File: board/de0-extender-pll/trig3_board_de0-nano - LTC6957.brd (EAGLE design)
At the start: 160 x 75 mm, 92 parts, among them J12 4p-2.54, J13 BU-SMB-V, J17 2p-2.54, J23 2p-2.54, J24 2p-2.54, J3 4p-2.54, J32 2p-2.54, J33 2p-2.54, J34 2p-2.54, J38 2p-2.54, J39 2p-2.54, J42 2p-2.54, J43 2p-2.54, J5 2p-2.54, J6 2p-2.54, J7 4p-2.54, K15_R10P BU-SMB-V, K16_R10N BU-SMB-V, P11 BU-SMB-V, P15 BU-SMB-V, P16_R15N BU-SMB-V, P9 BU-SMB-V, T13_B20N BU-SMB-V, T9CLK_7N BU-SMB-V

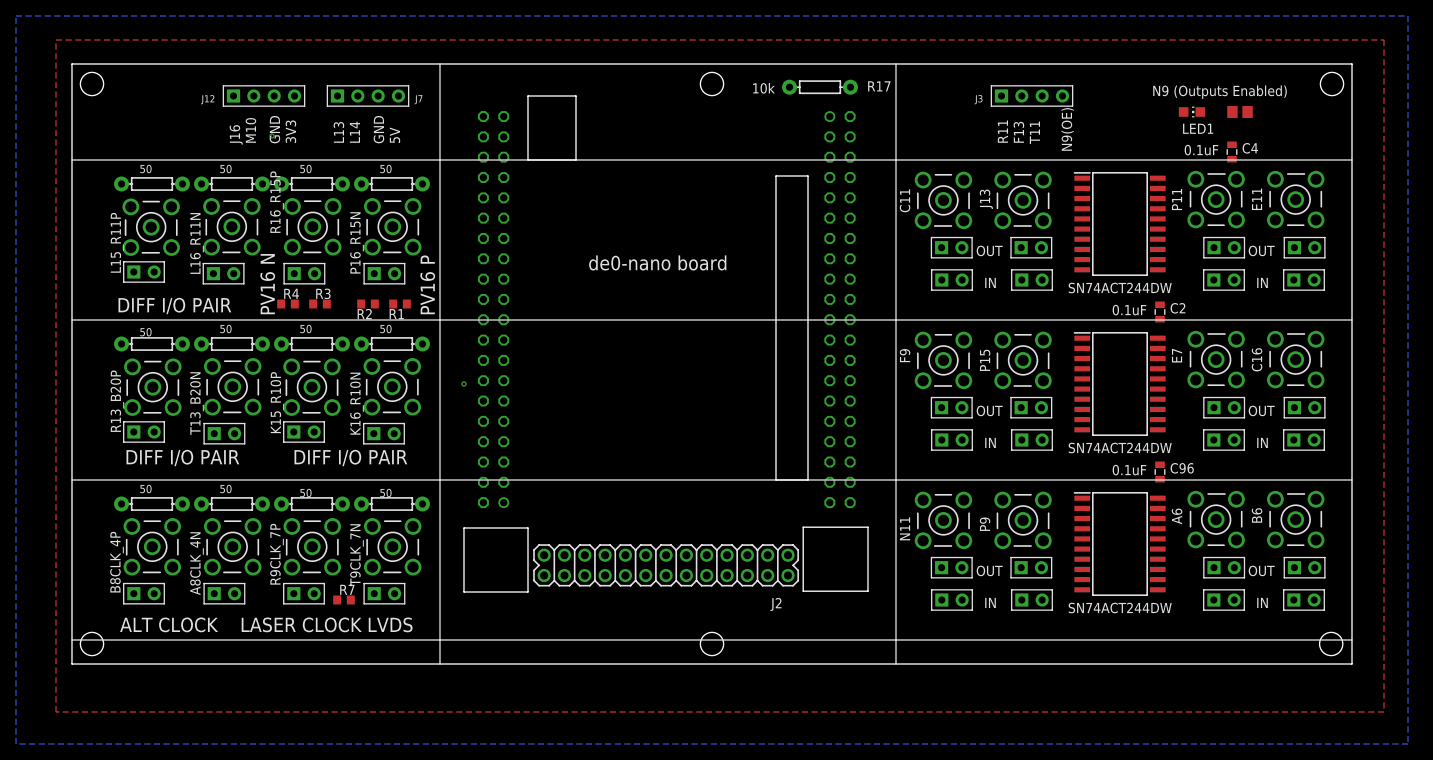
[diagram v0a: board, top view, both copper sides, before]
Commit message: fixed pecl termination
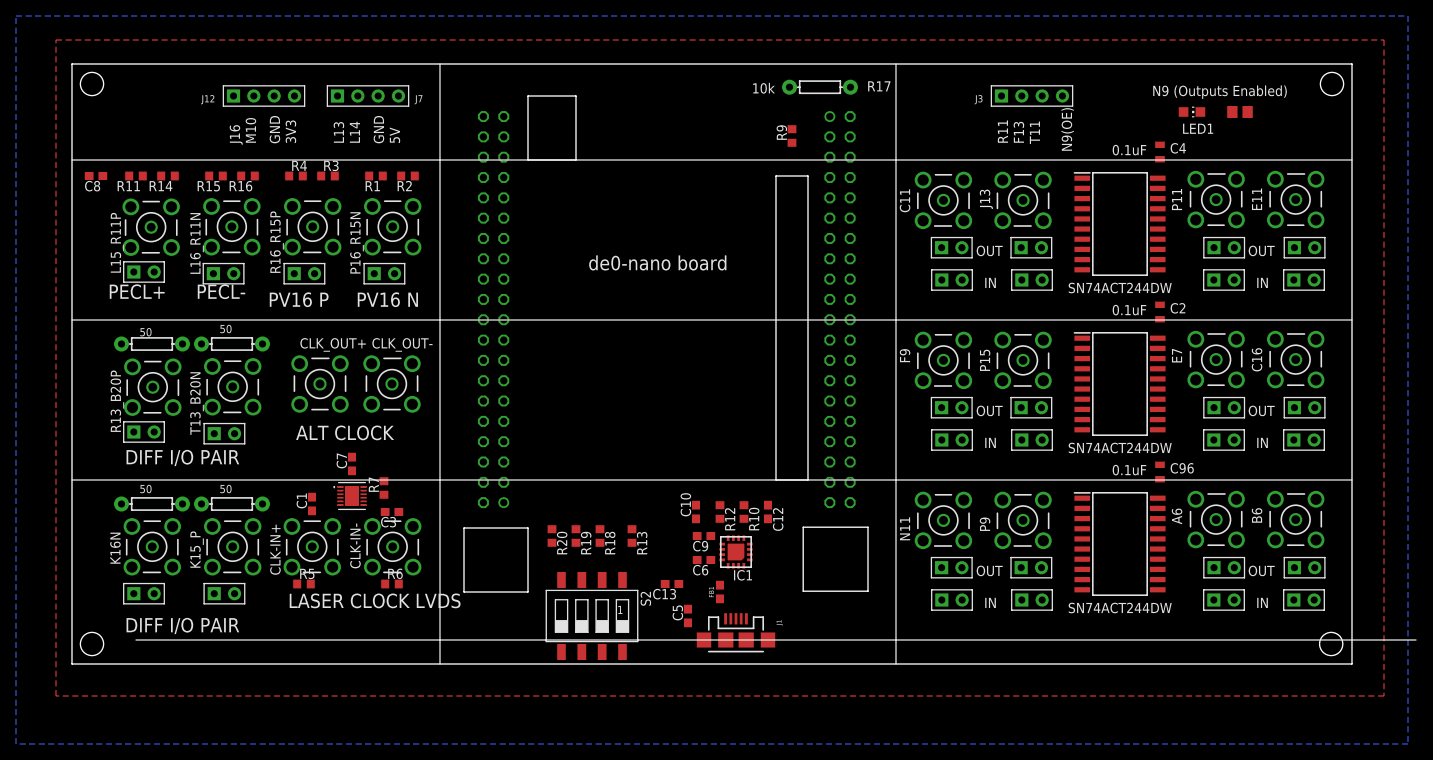
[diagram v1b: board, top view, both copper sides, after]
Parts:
- removed J2: (no value), SparkFun-Connectors:2X13
- removed J33, J39, J5, J6: 2p-2.54, Seeed-Connector:H2-2.54
- removed K15_R10P, K16_R10N: BU-SMB-V, con-coax:BU-SMB-V
- removed R28, R30, R31, R35, R41, R43: 50, SparkFun-Passives:AXIAL-0.3
- added C1, C3: 10 nF, rcl:C0603
- added C10, C12: 47pF, rcl:C0603
- added C13: 4.7 uF, rcl:C0603
- added C5, C6, C7, C8, C9: 0.1 uF, rcl:C0603
- added CLK_OUT+, CLK_OUT-: BU-SMB-V, con-coax:BU-SMB-V
- added FB1: 30Ω, SparkFun-Coils:0603
- added IC1: FT230XQ, ftdichip:QFN16
- added J1: (no value), SparkFun-Connectors:USB-MICROB
- added R10, R12: 27, rcl:R0603
- added R11, R16: 83, rcl:R0603
- added R13, R18, R19, R20: 330k, rcl:R0603
- added R14, R15: 130, rcl:R0603
- added R9: 100, rcl:R0603
- added S2: SWS004, smd-special:SMS-004
- added U1: LTC6957IDD-2TRPBF, ltc6957-2:DFN-12_DD_LIT
- R5, R6: value 50 -> 49.9; device SparkFun-Passives:AXIAL-0.3 -> rcl:R0603
- moved R2 16.8 mm to (-3.00, 97.0)
- moved R1 16.3 mm to (-7.00, 97.0)
- moved R3 16.0 mm to (-13.0, 97.0)
- moved R4 16.0 mm to (-17.0, 97.0)
- moved R7 14.9 mm to (-6.00, 58.0), turned to 90 degrees
- moved R5 10.0 mm to (-16.0, 46.0), turned to 0 degrees
- moved R6 10.0 mm to (-5.00, 46.0), turned to 0 degrees
- moved C4 9.00 mm to (91.0, 100.0)
- renumbered A8CLK_4N to K15_P, B8CLK_4P to K16N, R9CLK_7P to CLK-IN+, T9CLK_7N to CLK-IN-
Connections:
- new net N$1: J17.1, R13_B20P.2, R13_B20P.3, R13_B20P.4, R13_B20P.5, R161.P$1
- new net N$11: C10.2, J1.D-, R12.1
- new net N$12: IC1.6, R10.2
- new net N$13: IC1.7, R12.2
- new net N$14: C9.1, IC1.1, IC1.8, IC1.9
- new net N$15: R13.2, S2.1, U1.1
- new net N$16: R18.2, S2.2, U1.6
- new net N$17: R19.2, S2.3, U1.12
- new net N$18: R20.2, S2.4, U1.7
- new net N$2: C1.1, CLK-IN+.1, R5.2
- new net N$3: C3.1, CLK-IN-.1, R6.2
- new net N$4: C1.2, U1.3
- new net N$5: C3.2, U1.4
- new net N$6: C5.2, FB1.1, J1.VBUS
- new net N$7: C12.1, J1.D+, R10.1
- net 3V3: now also C7.1, C8.1, R14.1, R15.2, R4.1, S2.5, S2.6, S2.7, S2.8, U1.2; no longer R3.2
- net 5V: now also C13.1, C6.1, FB1.2, IC1.10
- net GND: now also C10.1, C12.2, C13.2, C5.1, C6.2, C7.2, C8.2, C9.2, CLK_OUT+.2, CLK_OUT+.3, CLK_OUT+.4, CLK_OUT+.5, CLK_OUT-.2, CLK_OUT-.3, CLK_OUT-.4, CLK_OUT-.5, IC1.13, IC1.2, IC1.3, J1.GND, R11.2, R13.1, R16.1, R18.1, R19.1, R20.1, R3.2, R5.1, R6.1, U1.13, U1.5; no longer J17.1, J33.1, J39.1, J5.1, J6.1, K15_R10P.2, K15_R10P.3, K15_R10P.4, K15_R10P.5, K16_R10N.2, K16_R10N.3, K16_R10N.4, K16_R10N.5, R13_B20P.2, R13_B20P.3, R13_B20P.4, R13_B20P.5, R161.P$1, R28.P$1, R30.P$1, R31.P$1, R35.P$1, R4.1, R41.P$1, R43.P$1, R5.P$1, R6.P$1
- net GPIO_0_IN0_A8CLK: now also CLK_OUT-.1, R9.2, U1.9; no longer J24.2, K15_P.1, R23.P$2
- net GPIO_0_IN1_B8CLK: now also CLK_OUT+.1, R9.1, U1.8; no longer J23.2, K16N.1, R22.P$2
- net GPIO_116_L16: now also R15.1, R16.2; no longer R28.P$2
- net GPIO_117_K16: now also J23.2, K16N.1, R22.P$2; no longer J33.2, K16_R10N.1, R30.P$2
- net GPIO_118_R16: no longer R31.P$2
- net GPIO_119_L15: now also R11.1, R14.2; no longer R43.P$2
- net GPIO_121_P16: no longer R41.P$2
- net GPIO_130_J16: now also IC1.15
- net GPIO_131_K15: now also J24.2, K15_P.1, R23.P$2; no longer J39.2, K15_R10P.1, R35.P$2
- net GPIO_1_IN0_T9CLK: now also U1.10; no longer CLK-IN-.1, J6.2, R6.P$2
- net GPIO_1_IN1_R9CLK: now also U1.11; no longer CLK-IN+.1, J5.2, R5.P$2
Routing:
- net GPIO_131_K15: track 53.1 -> 0.00 mm, vias 1 -> 0
- net GPIO_1_IN1_R9CLK: track 27.3 -> 0.00 mm
- net GPIO_118_R16: track 24.9 -> 0.00 mm
- net GPIO_117_K16: track 20.7 -> 0.00 mm, vias 1 -> 0
- net GPIO_1_IN0_T9CLK: track 16.2 -> 0.00 mm
- net GPIO_121_P16: track 11.9 -> 0.00 mm
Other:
- board text added: "PECL+"
- board text added: "PECL-"

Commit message: more work on board
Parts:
- VSLUE5, VSLUE7, VSLUE9: value SN74ACT244DW -> SN74LVTH244ARGYR; device SN74ACT244DW:SOIC127P1030X265-20N -> sn74lvth244argyr:RGY20_3P05X2P05
- moved C2 5.66 mm to (87.0, 76.0)
- moved C4 5.66 mm to (87.0, 96.0)
- moved C96 5.66 mm to (87.0, 56.0)
- moved R14 5.00 mm to (-38.0, 97.0)
- moved R11 3.00 mm to (-34.0, 97.0)
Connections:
- net 3V3: now also C2.2, C4.2, C96.2, VSLUE5.20, VSLUE7.20, VSLUE9.20
- net 5V: no longer C2.2, C4.2, C96.2, VSLUE5.20, VSLUE7.20, VSLUE9.20
- net GND: now also VSLUE5.21, VSLUE7.21, VSLUE9.21

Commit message: ready to autoroute
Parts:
- moved C8 50.0 mm to (-15.2, 54.8), turned to 0 degrees
- moved R7 18.6 mm to (12.5, 57.2)
- moved C1 6.54 mm to (-12.3, 50.0), turned to 270 degrees
- moved CLK-IN- 6.48 mm to (-3.64, 44.3)
- moved CLK-IN+ 6.38 mm to (-14.3, 44.3)
- moved C7 5.56 mm to (-14.6, 57.9), turned to 180 degrees
- moved R9 5.43 mm to (39.9, 103.9)
- moved C3 5.03 mm to (-6.09, 50.1), turned to 90 degrees
- moved R6 4.34 mm to (-3.53, 50.1), turned to 270 degrees
- moved R5 4.19 mm to (-14.9, 50.0), turned to 90 degrees
- moved R11 1.36 mm to (-32.7, 96.7), turned to 0 degrees
- moved R14 0.54 mm to (-37.6, 96.7), turned to 0 degrees
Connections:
- net 3V3: now also R17.P$1
- net 5V: no longer R17.P$1
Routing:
- net 5V: track 0.00 -> 154.4 mm, vias 0 -> 4
- net GPIO_0_IN1_B8CLK: track 0.00 -> 122.2 mm, vias 0 -> 3
- net GPIO_0_IN0_A8CLK: track 0.00 -> 110.9 mm, vias 0 -> 3
- net GPIO_119_L15: track 0.00 -> 57.9 mm, vias 0 -> 1
- net GPIO_116_L16: track 0.00 -> 50.2 mm, vias 0 -> 1
- net GPIO_118_R16: track 0.00 -> 39.6 mm, vias 0 -> 1
- net GPIO_121_P16: track 0.00 -> 26.6 mm, vias 0 -> 1
- net N$11: track 0.00 -> 18.8 mm, vias 0 -> 2
- net GPIO_1_IN1_R9CLK: track 0.00 -> 18.5 mm, vias 0 -> 1
- net GPIO_1_IN0_T9CLK: track 0.00 -> 18.4 mm, vias 0 -> 1
- net N$7: track 0.00 -> 18.0 mm, vias 0 -> 2
- net N$14: track 0.00 -> 15.0 mm, vias 0 -> 3
- net N$6: track 0.00 -> 7.33 mm
- net N$13: track 0.00 -> 3.12 mm
- net N$12: track 0.00 -> 2.70 mm
- added copper zone on layer 15, net 3V3
- added copper zone on layer 2, net 3V3
- added copper zone on layer 1, net GND
- removed copper zone on layer 1, net 5V

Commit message: autoroute attempt 2
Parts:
- removed OJ45, OJ46, OJ47, OJ48, OJ61, OJ62, OJ63, OJ64, OJ77, OJ78, OJ79, OJ80: 2p-2.54, Seeed-Connector:H2-2.54
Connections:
- net GND: no longer OJ45.2, OJ46.2, OJ47.2, OJ48.2, OJ61.2, OJ62.2, OJ63.2, OJ64.2, OJ77.2, OJ78.2, OJ79.2, OJ80.2
- net GPIO_010_B6: no longer OJ47.1
- net GPIO_011_A6: no longer OJ48.1
- net GPIO_018_E7: no longer OJ64.1
- net GPIO_022_F9: no longer OJ62.1
- net GPIO_026_E11: no longer OJ79.1
- net GPIO_028_C11: no longer OJ78.1
- net GPIO_110_P11: no longer OJ80.1
- net GPIO_113_P9: no longer OJ45.1
- net GPIO_115_N11: no longer OJ46.1
- net GPIO_120_P15: no longer OJ61.1
- net GPIO_132_J13: no longer OJ77.1
- net GPIO_23_C16: no longer OJ63.1
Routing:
- net GND: track 0.00 -> 8.69 mm, vias 0 -> 6
- net 3V3: track 0.00 -> 3.21 mm, vias 0 -> 4
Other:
- board text removed: "IN"

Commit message: Update trig3_board_de0-nano - LTC6957.brd
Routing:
- net 3V3: track 3.21 -> 13.8 mm, vias 4 -> 6
- net GND: track 8.69 -> 17.2 mm, vias 6 -> 9
- net GPIO_028_C11: track 0.00 -> 5.74 mm, vias 0 -> 2
- net GPIO_022_F9: track 0.00 -> 5.12 mm, vias 0 -> 2
- net GPIO_115_N11: track 0.00 -> 4.49 mm, vias 0 -> 2
- net OUT22: track 0.00 -> 4.03 mm, vias 0 -> 1
- net GPIO_113_P9: track 0.00 -> 4.03 mm, vias 0 -> 1
- net OUT39: track 0.00 -> 3.45 mm, vias 0 -> 2
- net OUT31: track 0.00 -> 3.45 mm, vias 0 -> 2
- net OUT23: track 0.00 -> 3.45 mm, vias 0 -> 2
- net OUT37: track 0.00 -> 2.55 mm, vias 0 -> 2
- net OUT29: track 0.00 -> 2.55 mm, vias 0 -> 2
- net OUT21: track 0.00 -> 2.55 mm, vias 0 -> 2
- net GPIO_114_N9: track 0.00 -> 2.48 mm, vias 0 -> 3
- net OUT38: track 0.00 -> 1.72 mm, vias 0 -> 1
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
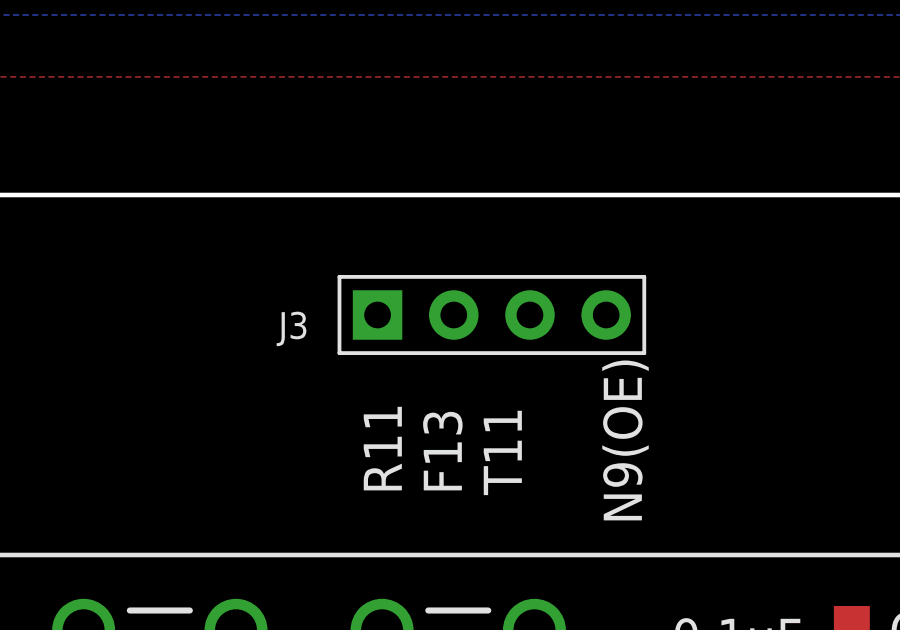
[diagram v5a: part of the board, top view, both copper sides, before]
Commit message: removed unnecessary header
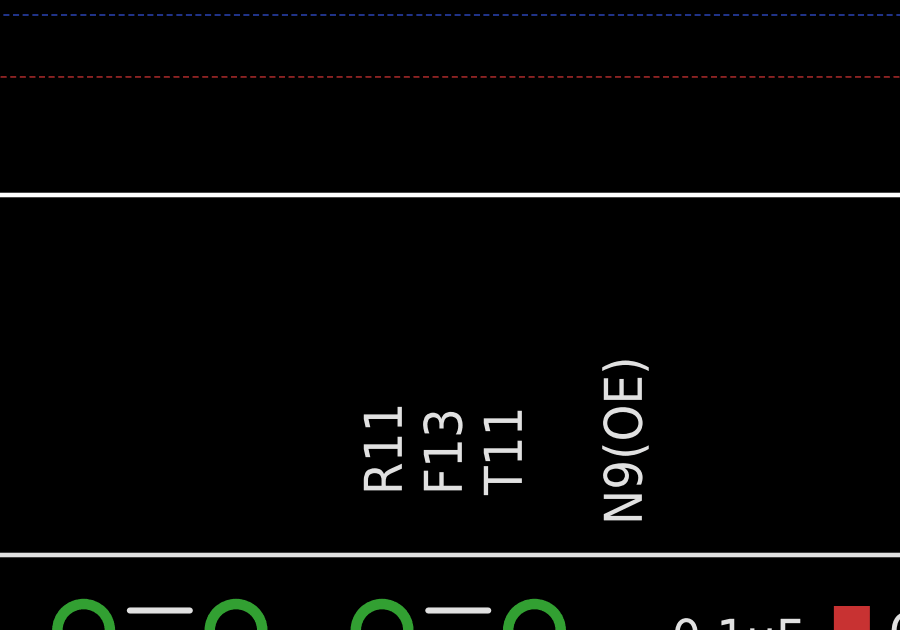
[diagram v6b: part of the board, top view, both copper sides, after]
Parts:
- removed J3: 4p-2.54, Seeed-Connector:H4-2.54
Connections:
- net GPIO_10_F13: no longer J3.2
- net GPIO_114_N9: no longer J3.4
- net GPIO_17_T11: no longer J3.3
- net GPIO_19_R11: no longer J3.1
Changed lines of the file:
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@@
 <attribute name="VALUE" x="-24.968" y="78.381" size="1.016" layer="21" font="vector" ratio="15" rot="R180"/>
-</element>
-<element name="J3" library="Seeed-Connector" library_urn="urn:adsk.eagle:library:478" package="H4-2.54" package3d_urn="urn:adsk.eagle:package:33137/1" value="4p-2.54" x="75" y="107" smashed="yes" rot="R90">
-<attribute name="MPN" value="F185-1104A1BSYA1" x="75" y="107" size="1.27" layer="27" rot="R90" display="off"/>
-<attribute name="NAME" x="68.905" y="107.095" size="0.889" layer="25" ratio="11" rot="R180"/>
 </element>
 <element name="LED1" library="led" library_urn="urn:adsk.eagle:library:259" package="CHIP-LED0805" package3d_urn="urn:adsk.eagle:package:15818/2" value="red" x="95" y="105" smashed="yes" rot="R270">
@@
 </elements>
 <signals>
-<signal name="GND">
+<signal name="GND" airwireshidden="yes">
 <polygon width="0.4064" layer="16">
 <vertex x="122" y="117"/>
@@
 <wire x1="49.73" y1="71.41" x2="86.75" y2="68.775" width="0" layer="19" extent="1-1"/>
 </signal>
-<signal name="3V3" class="1">
+<signal name="3V3" class="1" airwireshidden="yes">
 <contactref element="SV1" pad="29"/>
 <contactref element="SV2" pad="29"/>
@@
 <signal name="GPIO_10_F13">
 <contactref element="SV2" pad="2"/>
-<contactref element="J3" pad="2"/>
-<wire x1="6.43" y1="56.17" x2="73.73" y2="107" width="0" layer="19" extent="1-1"/>
 </signal>
 <signal name="GPIO_11_T15">
@@
 <signal name="GPIO_17_T11">
 <contactref element="SV2" pad="10"/>
-<contactref element="J3" pad="3"/>
-<wire x1="6.43" y1="66.33" x2="76.27" y2="107" width="0" layer="19" extent="1-1"/>
 </signal>
 <signal name="GPIO_19_R11">
 <contactref element="SV2" pad="14"/>
-<contactref element="J3" pad="1"/>
-<wire x1="6.43" y1="71.41" x2="71.19" y2="107" width="0" layer="19" extent="1-1"/>
 </signal>
 <signal name="GPIO_111_R10">
@@
 <contactref element="VSLUE7" pad="1"/>
 <contactref element="VSLUE9" pad="1"/>
-<contactref element="J3" pad="4"/>
 <contactref element="LED1" pad="A"/>
 <wire x1="87.725" y1="92.75" x2="88.553090625" y2="92.75" width="0.1524" layer="1"/>
@@
 <wire x1="87.725" y1="52.75" x2="88.553090625" y2="52.75" width="0.1524" layer="1"/>
 <via x="88.553090625" y="52.75" extent="1-16" drill="0.35"/>
+<contactref element="VSLUE5" pad="19"/>
 <wire x1="88.553090625" y1="92.75" x2="93.95" y2="105" width="0" layer="19" extent="1-1"/>
 <wire x1="85.25" y1="93.225" x2="87.725" y2="92.75" width="0" layer="19" extent="1-1"/>
-<wire x1="78.81" y1="107" x2="85.25" y2="93.225" width="0" layer="19" extent="1-1"/>
 <wire x1="85.25" y1="73.225" x2="87.725" y2="92.75" width="0" layer="19" extent="1-1"/>
 <wire x1="87.725" y1="72.75" x2="85.25" y2="73.225" width="0" layer="19" extent="1-1"/>
 <wire x1="85.25" y1="53.225" x2="87.725" y2="72.75" width="0" layer="19" extent="1-1"/>
 <wire x1="87.725" y1="52.75" x2="85.25" y2="53.225" width="0" layer="19" extent="1-1"/>
-<wire x1="52.31" y1="108.1" x2="78.81" y2="107" width="0" layer="19" extent="1-1"/>
+<wire x1="52.31" y1="108.1" x2="85.25" y2="93.225" width="0" layer="19" extent="1-1"/>
 <wire x1="8.97" y1="79.03" x2="52.31" y2="108.1" width="0" layer="19" extent="1-1"/>
-<contactref element="VSLUE5" pad="19"/>
 </signal>
 <signal name="GPIO_116_L16">
